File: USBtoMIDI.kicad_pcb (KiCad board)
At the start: 2 copper layers, 100 x 100 mm, 71 parts, among them J1 Conn_01x03, J2 Conn_01x03, J3 Conn_01x03, J7 Conn_02x04_Odd_Even, J8 Conn_01x05, J9 Conn_01x09, Q1 2N2219, Q2 2N2219, Q3 2N2219, Q4 2N2219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

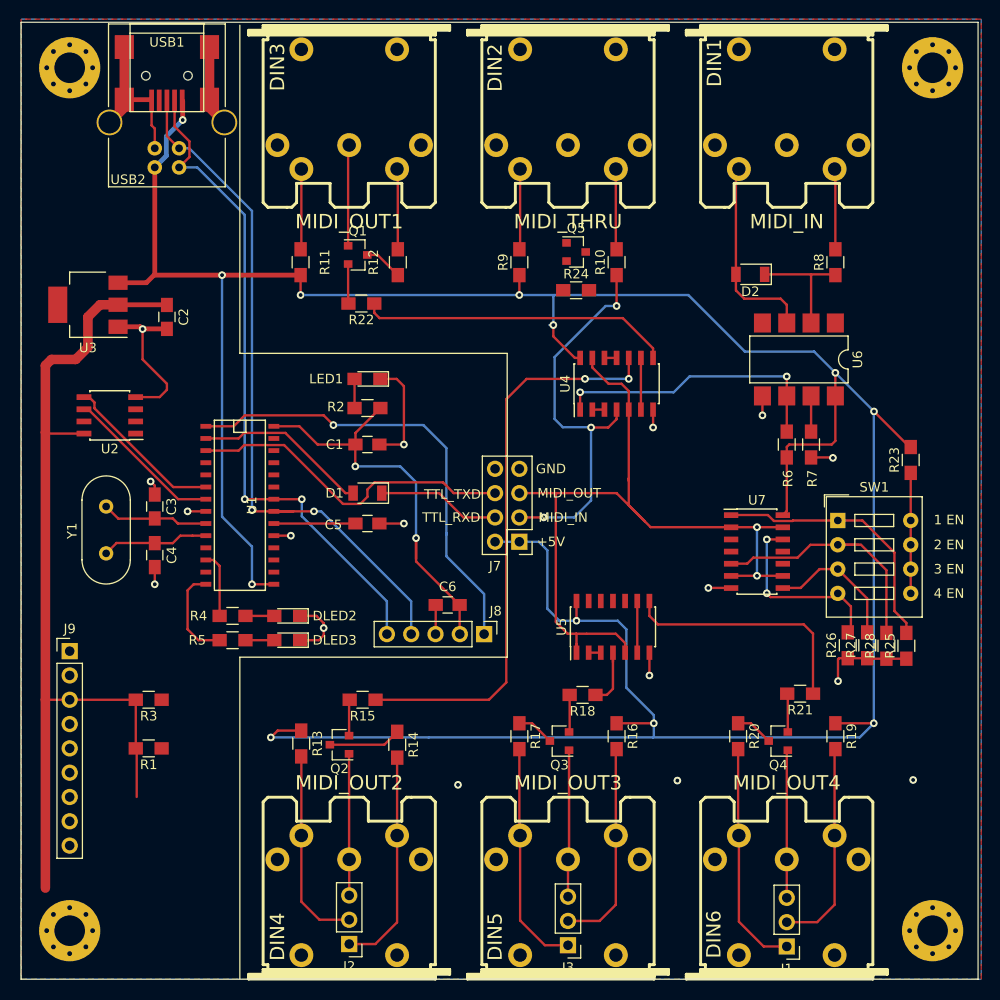
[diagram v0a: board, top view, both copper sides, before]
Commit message: changed usb type
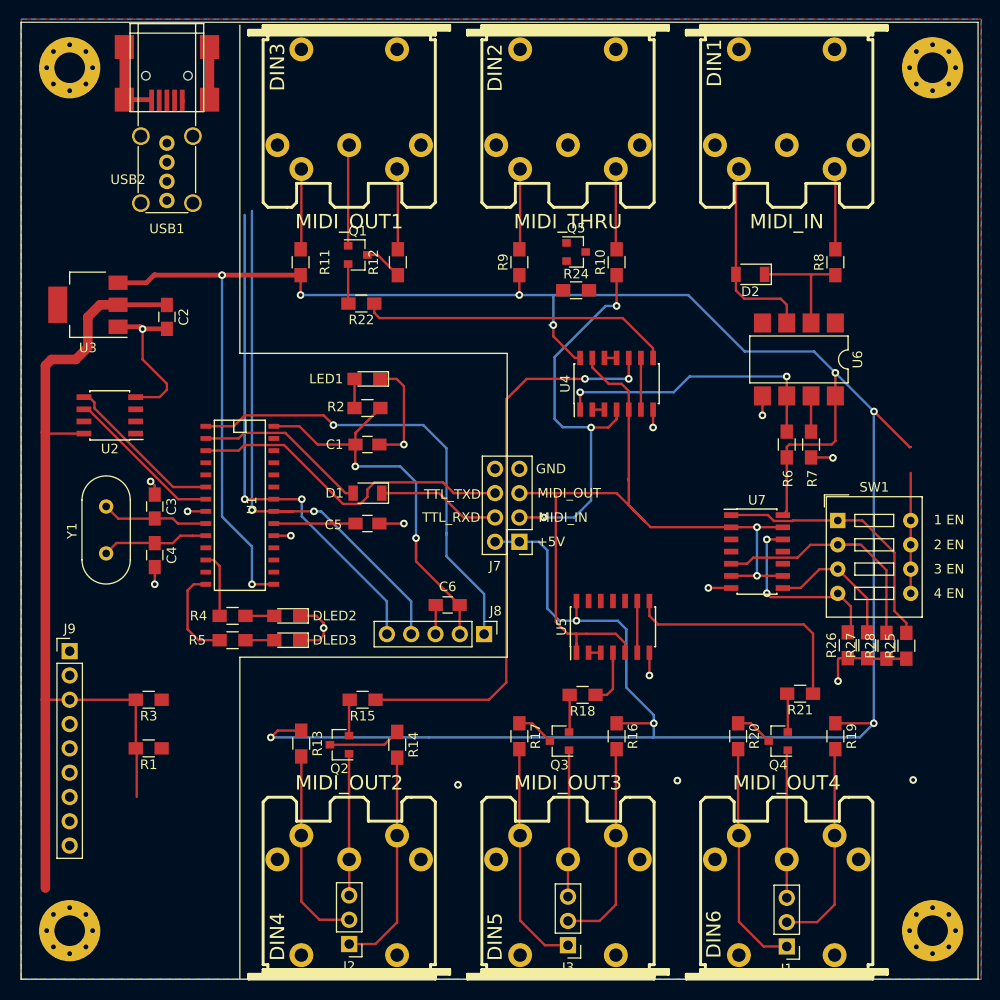
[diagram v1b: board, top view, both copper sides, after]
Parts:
- removed R23: 470R, Resistors_SMD:R_0805_HandSoldering
- USB1: footprint Connectors:USB_B -> Connectors:USB_A_Vertical
- moved USB1 2.84 mm to (123.2, 58.7), turned to 0 degrees
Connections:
- SW1 pad 5: Net-(R23-Pad1) -> +5V
- SW1 pad 6: Net-(R23-Pad1) -> +5V
- SW1 pad 7: Net-(R23-Pad1) -> +5V
- SW1 pad 8: Net-(R23-Pad1) -> +5V
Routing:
- net USB_D-: track 70.4 -> 53.5 mm
- net USB_D+: track 73.1 -> 57.3 mm
- net Net-(R23-Pad1): track 12.6 -> 0.00 mm
- net GND: track 148.8 -> 137.7 mm
- net +5V: track 320.9 -> 314.2 mm, vias 12 -> 11

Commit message: update config ports
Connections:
- J7 pad 1: +5V -> MIDI_IN
- J7 pad 2: +5V -> TTL_RXD
- J7 pad 3: MIDI_IN -> Net-(J7-Pad3)
- J7 pad 4: TTL_RXD -> Net-(J7-Pad4)
- J7 pad 5: MIDI_OUT -> MIDI_IN
- J7 pad 6: TTL_TXD -> Net-(J7-Pad6)
- J7 pad 7: GND -> MIDI_OUT
- J7 pad 8: GND -> TTL_TXD
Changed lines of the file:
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@@
     (zones 0)
     (modules 70)
-    (nets 91)
+    (nets 94)
   )
   (page A4)
@@
   (net 89 "Net-(Q5-Pad3)")
   (net 90 "Net-(Q3-Pad1)")
+  (net 91 "Net-(J7-Pad3)")
+  (net 92 "Net-(J7-Pad4)")
+  (net 93 "Net-(J7-Pad6)")
   (net_class Default "This is the default net class."
     (clearance 0.2)
@@
     (add_net "Net-(DLED2-Pad2)")
     (add_net "Net-(DLED3-Pad2)")
+    (add_net "Net-(J7-Pad3)")
+    (add_net "Net-(J7-Pad4)")
+    (add_net "Net-(J7-Pad6)")
     (add_net "Net-(LED1-Pad2)")
     (add_net "Net-(Q1-Pad2)")
@@
     )
     (pad 1 thru_hole rect (at 0 0 180) (size 1.7 1.7) (drill 1) (layers *.Cu *.Mask)
-      (net 6 +5V))
+      (net 41 MIDI_IN))
     (pad 2 thru_hole oval (at 2.54 0 180) (size 1.7 1.7) (drill 1) (layers *.Cu *.Mask)
-      (net 6 +5V))
+      (net 31 TTL_RXD))
     (pad 3 thru_hole oval (at 0 2.54 180) (size 1.7 1.7) (drill 1) (layers *.Cu *.Mask)
+      (net 91 "Net-(J7-Pad3)"))
+    (pad 4 thru_hole oval (at 2.54 2.54 180) (size 1.7 1.7) (drill 1) (layers *.Cu *.Mask)
+      (net 92 "Net-(J7-Pad4)"))
+    (pad 5 thru_hole oval (at 0 5.08 180) (size 1.7 1.7) (drill 1) (layers *.Cu *.Mask)
       (net 41 MIDI_IN))
-    (pad 4 thru_hole oval (at 2.54 2.54 180) (size 1.7 1.7) (drill 1) (layers *.Cu *.Mask)
-      (net 31 TTL_RXD))
-    (pad 5 thru_hole oval (at 0 5.08 180) (size 1.7 1.7) (drill 1) (layers *.Cu *.Mask)
+    (pad 6 thru_hole oval (at 2.54 5.08 180) (size 1.7 1.7) (drill 1) (layers *.Cu *.Mask)
+      (net 93 "Net-(J7-Pad6)"))
+    (pad 7 thru_hole oval (at 0 7.62 180) (size 1.7 1.7) (drill 1) (layers *.Cu *.Mask)
       (net 42 MIDI_OUT))
-    (pad 6 thru_hole oval (at 2.54 5.08 180) (size 1.7 1.7) (drill 1) (layers *.Cu *.Mask)
+    (pad 8 thru_hole oval (at 2.54 7.62 180) (size 1.7 1.7) (drill 1) (layers *.Cu *.Mask)
       (net 32 TTL_TXD))
-    (pad 7 thru_hole oval (at 0 7.62 180) (size 1.7 1.7) (drill 1) (layers *.Cu *.Mask)
-      (net 3 GND))
-    (pad 8 thru_hole oval (at 2.54 7.62 180) (size 1.7 1.7) (drill 1) (layers *.Cu *.Mask)
-      (net 3 GND))
     (model ${KISYS3DMOD}/Pin_Headers.3dshapes/Pin_Header_Straight_2x04_Pitch2.54mm.wrl
       (at (xyz 0 0 0))

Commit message: update logic
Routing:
- net MIDI_IN: track 42.4 -> 49.4 mm
- net +5V: track 314.2 -> 308.4 mm
- net TTL_RXD: track 12.9 -> 15.0 mm
- net MIDI_OUT: track 85.4 -> 87.4 mm
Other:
- board text added: "1-2 Send MIDI to uC 5-7 Loop MIDI to Outputs 7-8 Send MIDI from uC"
- board text removed: "+5V"
- board text removed: "GND"

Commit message: updates
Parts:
- D1: footprint Diodes_SMD:D_1206 -> Diodes_SMD:D_SOD-323
- U4, U5: value 74HC14 -> 74AS14
- U6: footprint Housings_DIP:SMDIP-8_W7.62mm -> Housings_DIP:DIP-8_W7.62mm
- U7: value 4081 -> 74HC08
- moved R1 38.7 mm to (156.3, 105.4), turned to 90 degrees
- moved R3 28.9 mm to (124.2, 88.1), turned to 90 degrees
- moved U3 13.8 mm to (113.3, 61.8), turned to 90 degrees
- moved C2 13.7 mm to (111.0, 70.6), turned to 90 degrees
- moved R11 10.2 mm to (147.3, 70.4)
- moved R12 10.2 mm to (137.2, 70.4)
- moved R9 10.2 mm to (170.2, 71.1)
- moved R16 10.1 mm to (160.1, 121.4)
- moved R17 10.1 mm to (170.1, 121.4)
- moved R20 10.1 mm to (192.9, 121.3)
- moved R19 10.1 mm to (183.0, 121.3)
- moved R10 10.0 mm to (160.1, 71.1)
- moved U6 5.39 mm to (193.0, 77.5)
- moved U4 3.11 mm to (167.1, 84.5)
- moved U5 2.74 mm to (167.1, 108.6)
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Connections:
- Q3 pad 1: Net-(Q3-Pad1) -> GND
- R24 pad 1: MIDI_IN -> Net-(R24-Pad1)
- U4 pad 10: Net-(R15-Pad1) -> Net-(R22-Pad1)
- U4 pad 2: Net-(U4-Pad2) -> MIDI_IN
- U4 pad 3: Net-(U4-Pad2) -> GND
- U4 pad 4: MIDI_IN -> GND
- U4 pad 5: Net-(U4-Pad5) -> MIDI_IN
- U4 pad 8: Net-(R22-Pad1) -> Net-(R24-Pad1)
- U5 pad 10: (no net) -> Net-(R18-Pad1)
- U5 pad 11: (no net) -> Net-(U5-Pad11)
- U5 pad 12: (no net) -> Net-(U5-Pad11)
- U5 pad 13: (no net) -> Net-(U5-Pad13)
- U5 pad 4: Net-(R18-Pad1) -> Net-(R15-Pad1)
- U7 pad 10: Net-(U5-Pad1) -> Net-(U5-Pad13)
- U7 pad 3: Net-(U4-Pad5) -> Net-(U4-Pad13)
- U7 pad 4: Net-(U4-Pad13) -> Net-(U5-Pad1)
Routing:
- net +5V: track 308.4 -> 88.5 mm, vias 11 -> 8
- net +3V3: track 139.1 -> 11.6 mm
- net TTL_RXD: track 15.0 -> 82.4 mm, vias 0 -> 2
- net TTL_TXD: track 35.0 -> 95.4 mm, vias 0 -> 4
- net GND: track 137.7 -> 184.4 mm
- net SS: track 0.00 -> 42.0 mm, vias 0 -> 2
- net MIDI_OUT: track 87.4 -> 46.4 mm
- net SCL: track 0.00 -> 37.3 mm, vias 0 -> 2
- net SDA: track 0.00 -> 35.7 mm, vias 0 -> 2
- net SDO: track 0.00 -> 35.1 mm, vias 0 -> 3
- net Net-(U4-Pad13): track 0.00 -> 34.5 mm
- net Net-(R15-Pad1): track 59.9 -> 25.4 mm, vias 2 -> 0
- net Net-(U5-Pad5): track 0.00 -> 29.1 mm
- net Net-(U5-Pad1): track 0.00 -> 27.7 mm
- net Net-(U5-Pad13): track 0.00 -> 25.7 mm, vias 0 -> 2
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- added copper zone on F.Cu, net +3V3
- added copper zone on F.Cu, net +5V
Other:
- board text added: "1"
- board text added: "1-2 Send MIDI_IN to USB_HOST 5-7 Loop MIDI_IN to MIDI_OUT 7-8 Send USB_HOST to MIDI_OUT"
- board text added: "2"
- board text added: "3V3"
- board text added: "5"
- board text added: "5V"
- board text added: "7"
- board text added: "8"
- board text added: "USB_HOST"
- board text removed: "1-2 Send MIDI to uC 5-7 Loop MIDI to Outputs 7-8 Send MIDI from uC"

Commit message: silk updates
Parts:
- moved J8 3.43 mm to (156.3, 106.6)
- moved C6 2.18 mm to (150.0, 103.6), turned to 0 degrees
- moved R1 2.18 mm to (155.1, 103.6), turned to 180 degrees
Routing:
- net MCLR: track 49.8 -> 45.4 mm
- net USB_D-: track 73.8 -> 70.3 mm
- net USB_D+: track 78.1 -> 74.7 mm
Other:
- board text added: "+3V3"
- board text added: "+5V"
- board text added: "1-2 : Send MIDI_IN to USB_HOST 5-7 : Loop MIDI_IN to MIDI_OUT 7-8 : Send USB_HOST to MIDI_OUT"
- board text added: "GND"
- board text added: "MCLR"
- board text added: "MIDI MAYHEM 2021 v1.0 Isolated Through Isolated 4 Output w/disable USB Host Mode"
- board text added: "PROG"
- board text added: "RB10"
- board text added: "RB11"
- board text added: "SCL"
- board text added: "SDA"
- board text added: "SDO"
- board text added: "SS"
- board text added: "TTR_RXD"
- board text removed: "1-2 Send MIDI_IN to USB_HOST 5-7 Loop MIDI_IN to MIDI_OUT 7-8 Send USB_HOST to MIDI_OUT"

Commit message: updates
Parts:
- moved LED1 32.5 mm to (112.4, 76.2)
- moved R2 32.4 mm to (112.4, 79.8), turned to 180 degrees
- moved C1 13.8 mm to (130.9, 86.2), turned to 180 degrees
- moved R1 6.88 mm to (151.6, 97.7)
- moved D1 6.35 mm to (144.1, 88.9)
- moved C5 4.32 mm to (139.8, 98.6)
- moved C6 2.33 mm to (148.0, 102.5)
- moved J8 2.33 mm to (154.3, 105.4)
- moved U2 1.82 mm to (117.6, 88.9), turned to 0 degrees
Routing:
- net +3V3: track 11.6 -> 28.9 mm
- net GND: track 184.1 -> 170.9 mm, vias 14 -> 15
- net SDA2: track 17.0 -> 9.27 mm
- net Net-(C5-Pad2): track 8.53 -> 4.64 mm
- net Net-(D1-Pad2): track 22.5 -> 19.2 mm
- net TTL_TXD: track 95.4 -> 93.0 mm
- net SCL2: track 16.6 -> 14.5 mm
- net Net-(LED1-Pad2): track 3.05 -> 5.12 mm
- net USB_D+: track 74.7 -> 76.5 mm
- net MCLR: track 45.4 -> 47.1 mm, vias 1 -> 2
- net +5V: track 88.5 -> 89.6 mm
- net TTL_RXD: track 82.4 -> 82.0 mm, vias 2 -> 4
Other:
- board text added: "DISABLE OUTPUT"

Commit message: updates
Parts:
- R8: value 100R -> 220R
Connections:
- J7 pad 3: Net-(J7-Pad3) -> +5V
- J7 pad 4: Net-(J7-Pad4) -> GND
- J7 pad 6: Net-(J7-Pad6) -> GND
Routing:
- net GND: track 170.9 -> 177.9 mm
- net +5V: track 89.6 -> 94.0 mm, vias 8 -> 9
- net +3V3: track 28.9 -> 29.4 mm
